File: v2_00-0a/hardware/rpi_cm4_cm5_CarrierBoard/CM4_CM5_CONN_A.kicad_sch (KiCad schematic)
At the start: 2 parts, among them J6 DF40HC(3.0)-100DS-0.4V(58), U17 Raspberry PI CM4 and CM5 symb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

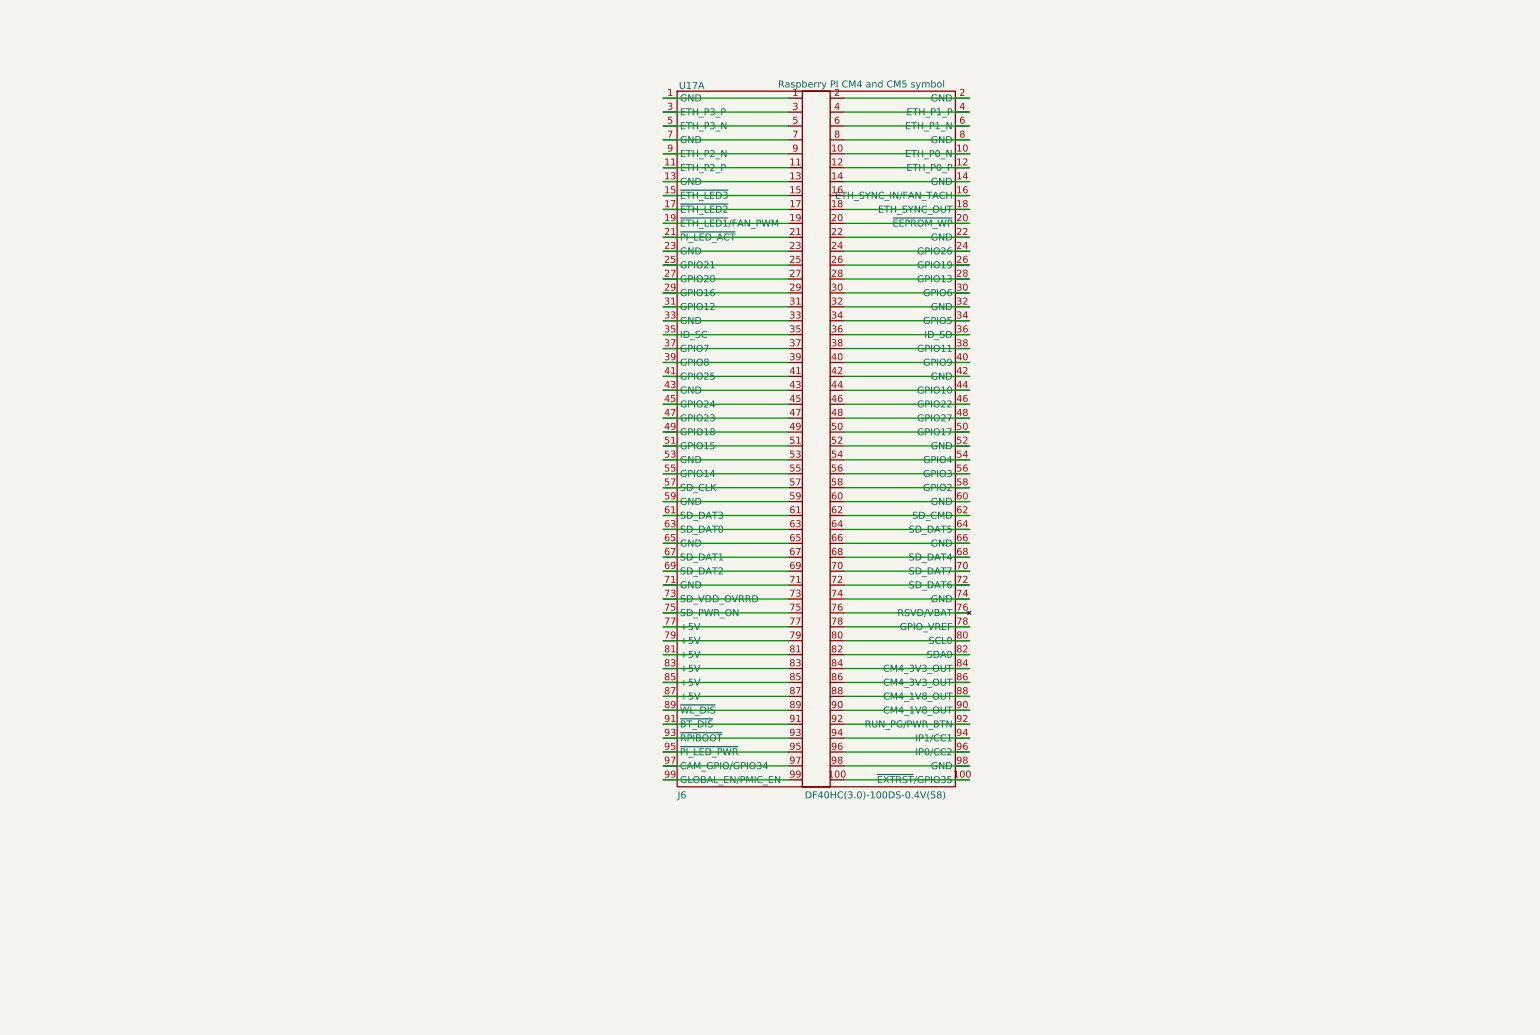
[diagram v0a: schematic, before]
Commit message: Update schematics (several new hierarchical pages, updates bus labels)
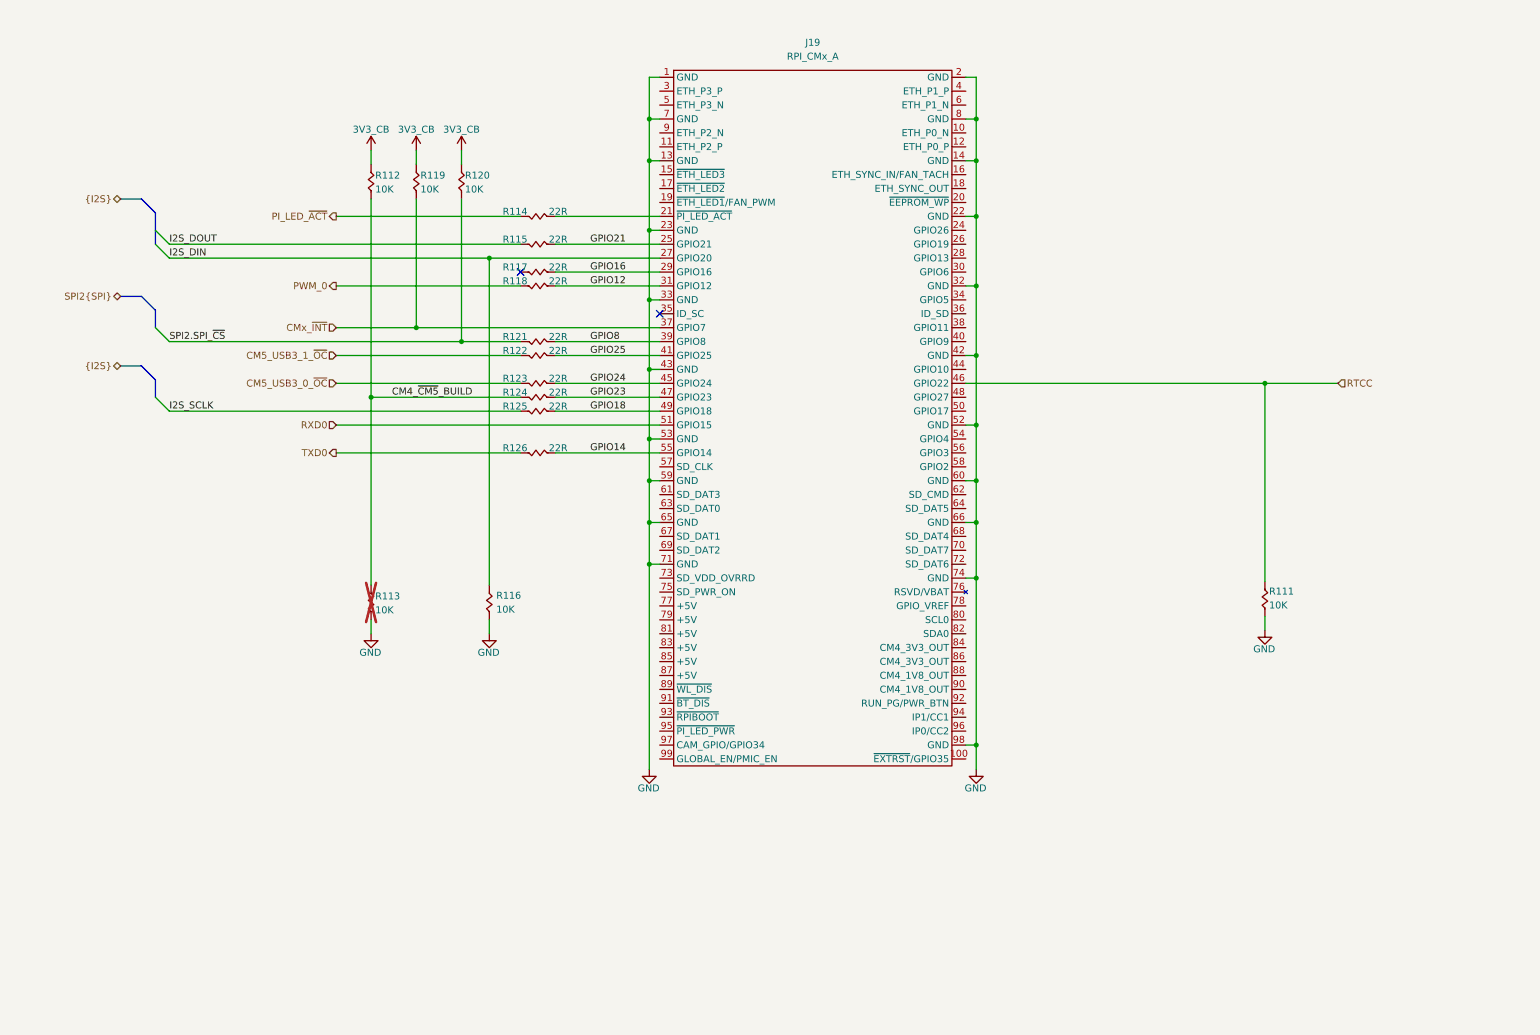
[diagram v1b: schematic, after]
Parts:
- removed J6: DF40HC(3.0)-100DS-0.4V(58), footprint:DF40HC(3.0)-100DS-0.4V, symbol KicadCompDb:Connector/CONN_00007
- removed U17: Raspberry PI CM4 and CM5 symbol, rPI_CM4_CM5, symbol KiCad_Lib_Symbols:RPI_CM4_CM5
- added J19: RPI_CMx_A, footprint:DF40HC(3.0)-100DS-0.4V, symbol KicadCompDb:Connector/CONN_00014
- added R111, R112, R113, R116, R119, R120: 10K, footprint:RES_0402, symbol KicadCompDb:Resistors/RES_SMT_00013
- added R114, R115, R117, R118, R121, R122, R123, R124, R125, R126: 22R, footprint:RES_0402, symbol KicadCompDb:Resistors/RES_SMT_00015
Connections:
- new net: J19.21 (~{PI_LED_ACT}), R114.1
- new net 3V3_CB: R112.2, R119.2, R120.2
- new net CM4_~{CM5}_BUILD: R112.1, R113.2, R124.2
- new net CM5_USB3_0_~{OC}: R123.2
- new net CM5_USB3_1_~{OC}: R122.2
- new net CMx_~{INT}: J19.37 (GPIO7), R119.1
- new net GND: J19.1 (GND), J19.13 (GND), J19.14 (GND), J19.2 (GND), J19.22 (GND), J19.23 (GND), J19.32 (GND), J19.33 (GND), J19.42 (GND), J19.43 (GND), J19.52 (GND), J19.53 (GND), J19.59 (GND), J19.60 (GND), J19.65 (GND), J19.66 (GND), J19.7 (GND), J19.71 (GND), J19.74 (GND), J19.8 (GND), J19.98 (GND), R111.1, R113.1, R116.1
- new net GPIO12: J19.31 (GPIO12), R118.1
- new net GPIO14: J19.55 (GPIO14), R126.1
- new net GPIO16: J19.29 (GPIO16), R117.1
- new net GPIO18: J19.49 (GPIO18), R125.1
- new net GPIO21: J19.25 (GPIO21), R115.1
- new net GPIO23: J19.47 (GPIO23), R124.1
- new net GPIO24: J19.45 (GPIO24), R123.1
- new net GPIO25: J19.41 (GPIO25), R122.1
- new net GPIO8: J19.39 (GPIO8), R121.1
- new net I2S_DIN: J19.27 (GPIO20), R116.2
- new net I2S_DOUT: R115.2
- new net I2S_SCLK: R125.2
- new net PI_LED_~{ACT}: R114.2
- new net PWM_0: R118.2
- new net RTCC: J19.46 (GPIO22), R111.2
- new net RXD0: J19.51 (GPIO15)
- new net SPI2.SPI_~{CS}: R120.1, R121.2
- new net TXD0: R126.2
- no-connect marks 0 -> 2

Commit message: Add new page and update schematics
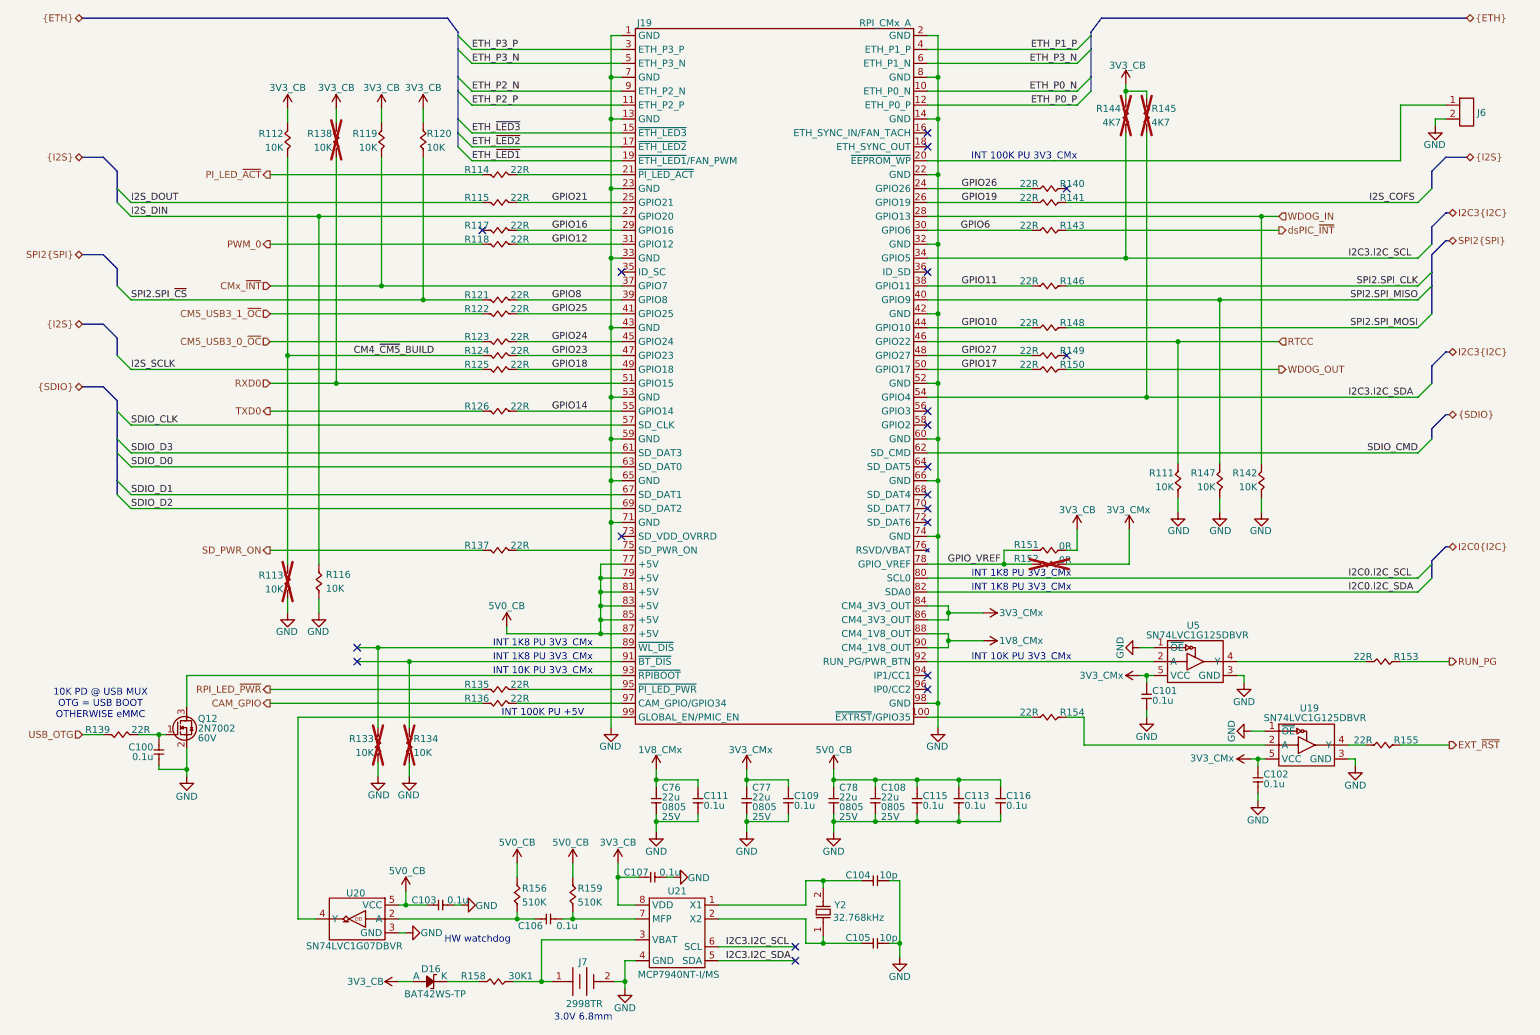
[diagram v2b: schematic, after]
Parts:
- added C100, C101, C102, C103, C106, C107, C109, C111, C113, C115, C116: 0.1u, footprint:CAP_NONPOL_0402, symbol KicadCompDb:Capacitors/CAP_CER_SMT_00001
- added C104, C105: 10p, footprint:CAP_NONPOL_0402, symbol KicadCompDb:Capacitors/CAP_CER_SMT_00006
- added C108, C76, C77, C78: 22u, footprint:CAP_NONPOL_0805, symbol KicadCompDb:Capacitors/CAP_CER_SMT_00011
- added D16: BAT42WS-TP, footprint:SOD-323, symbol KicadCompDb:Diodes/DIODE_00006
- added J6: M20-9990245, footprint:HEADER_2P_2_54MM, symbol KicadCompDb:Connector/CONN_00003
- added J7: 2998TR, 2998TR, symbol KicadCompDb:Miscellaneous/MISC_00005
- added Q12: 2N7002, footprint:SOT-23-3, symbol KicadCompDb:Mosfet/MOSFET_00001
- added R133, R134, R138, R142, R147: 10K, footprint:RES_0402, symbol KicadCompDb:Resistors/RES_SMT_00013
- added R135, R136, R137, R139, R140, R141, R143, R146, R148, R149, R150, R153, R154, R155: 22R, footprint:RES_0402, symbol KicadCompDb:Resistors/RES_SMT_00015
- added R144, R145: 4K7, footprint:RES_0402, symbol KicadCompDb:Resistors/RES_SMT_00010
- added R151, R152: 0R, footprint:RES_0402, symbol KicadCompDb:Resistors/RES_SMT_00001
- added R156, R159: 510K, footprint:RES_0402, symbol KicadCompDb:Resistors/RES_SMT_00020
- added R158: 30K1, footprint:RES_0402, symbol KicadCompDb:Resistors/RES_SMT_00016
- added U19, U5: SN74LVC1G125DBVR, footprint:SOT-23-5, symbol KicadCompDb:Logic/LOGIC_00001
- added U20: SN74LVC1G07DBVR, footprint:SOT-23-5, symbol KicadCompDb:Logic/LOGIC_00002
- added U21: MCP7940NT-I/MS, footprint:MSOP-8, symbol KicadCompDb:Digital/DIGITAL_00001
- added Y2: 32.768kHz, footprint:2-SMD_3_2mmx1_5mm, symbol KicadCompDb:Crystals/CRYSTAL_00003
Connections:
- net 3V3_CB: now also C107.1, D16.2 (A), R138.2, R144.2, R145.2, R151.2, U21.8 (VDD)
- net GND: now also C100.1, C101.1, C102.1, C103.2, C104.2, C105.2, C107.2, C108.1, C109.1, C111.1, C113.1, C115.1, C116.1, C76.1, C77.1, C78.1, J6.2, J7.2, Q12.2 (S), R133.1, R134.1, R142.1, R147.1, U19.1 (~{OE}), U19.3 (GND), U20.3 (GND), U21.4 (GND), U5.1 (~{OE}), U5.3 (GND)
- net RXD0: now also R138.1
- net ETH_P0_N: now reaches J19.10 (ETH_P0_N)
- net at J19.100 (~{EXTRST}/GPIO35): now also R154.1
- net ETH_P2_P: now reaches J19.11 (ETH_P2_P)
- net ETH_P0_P: now reaches J19.12 (ETH_P0_P)
- net ETH_~{LED3}: now reaches J19.15 (~{ETH_LED3})
- net ETH_~{LED2}: now reaches J19.17 (~{ETH_LED2})
- net ETH_~{LED1}: now reaches J19.19 (~{ETH_LED1}/FAN_PWM)
- net at J19.20 (~{EEPROM_WP}): now also J6.1
- net GPIO26: now reaches J19.24 (GPIO26)
- net GPIO26: now also R140.1
- net GPIO19: now reaches J19.26 (GPIO19)
- net GPIO19: now also R141.1
- net WDOG_IN: now reaches J19.28 (GPIO13)
- net WDOG_IN: now also R142.2
- net ETH_P3_P: now reaches J19.3 (ETH_P3_P)
- net GPIO6: now reaches J19.30 (GPIO6)
- net GPIO6: now also R143.1
- net I2C3.I2C_SCL: now reaches J19.34 (GPIO5)
- net I2C3.I2C_SCL: now also R144.1, U21.6 (SCL)
- net GPIO11: now reaches J19.38 (GPIO11)
- net GPIO11: now also R146.1
- net ETH_P1_P: now reaches J19.4 (ETH_P1_P)
- net SPI2.SPI_MISO: now reaches J19.40 (GPIO9)
- net SPI2.SPI_MISO: now also R147.2
- net GPIO10: now reaches J19.44 (GPIO10)
- net GPIO10: now also R148.1
- net GPIO27: now reaches J19.48 (GPIO27)
- net GPIO27: now also R149.1
- net ETH_P3_N: now reaches J19.5 (ETH_P3_N)
- net ETH_P3_N: now also J19.6 (ETH_P1_N)
- net GPIO17: now reaches J19.50 (GPIO17)
- net GPIO17: now also R150.1
- net I2C3.I2C_SDA: now reaches J19.54 (GPIO4)
- net I2C3.I2C_SDA: now also R145.1, U21.5 (SDA)
- net SDIO_CLK: now reaches J19.57 (SD_CLK)
- net SDIO_D3: now reaches J19.61 (SD_DAT3)
- net SDIO_CMD: now reaches J19.62 (SD_CMD)
- net SDIO_D0: now reaches J19.63 (SD_DAT0)
- net SDIO_D1: now reaches J19.67 (SD_DAT1)
- net SDIO_D2: now reaches J19.69 (SD_DAT2)
- net at J19.75 (SD_PWR_ON): now also R137.1
- net 5V0_CB: now reaches J19.77 (+5V)
- net 5V0_CB: now also J19.79 (+5V), J19.81 (+5V), J19.83 (+5V), J19.85 (+5V), J19.87 (+5V), C103.1, C108.2, C113.2, C115.2, C116.2, C78.2, R156.2, R159.2, U20.5 (VCC)
- net GPIO_VREF: now reaches J19.78 (GPIO_VREF)
- net GPIO_VREF: now also R151.1, R152.1
- net I2C0.I2C_SCL: now reaches J19.80 (SCL0)
- net I2C0.I2C_SDA: now reaches J19.82 (SDA0)
- net 3V3_CMx: now reaches J19.84 (CM4_3V3_OUT)
- net 3V3_CMx: now also J19.86 (CM4_3V3_OUT), C101.2, C102.2, C109.2, C77.2, R152.2, U19.5 (VCC), U5.5 (VCC)
- net 1V8_CMx: now reaches J19.88 (CM4_1V8_OUT)
- net 1V8_CMx: now also J19.90 (CM4_1V8_OUT), C111.2, C76.2
- net at J19.89 (~{WL_DIS}): now also R133.2
- net ETH_P2_N: now reaches J19.9 (ETH_P2_N)
- net at J19.91 (~{BT_DIS}): now also R134.2
- net at J19.92 (RUN_PG/PWR_BTN): now also U5.2 (A)
- net at J19.93 (~{RPIBOOT}): now also Q12.3 (D)
- net at J19.95 (~{PI_LED_PWR}): now also R135.1
- net at J19.97 (CAM_GPIO/GPIO34): now also R136.1
- net at J19.99 (GLOBAL_EN/PMIC_EN): now also U20.4 (Y)
- new net: R154.2, U19.2 (A)
- new net: J7.1, R158.1, U21.3 (VBAT)
- new net: D16.1 (K), R158.2
- new net: C106.1, R156.1, U20.2 (A)
- new net: C106.2, R159.1, U21.7 (MFP)
- new net: C104.1, U21.1 (X1), Y2.2 (XO)
- new net: R153.1, U5.4 (Y)
- new net: C105.1, U21.2 (X2), Y2.1 (XI)
- new net: R155.1, U19.4 (Y)
- new net: C100.2, Q12.1 (G), R139.1
- new net CAM_GPIO: R136.2
- new net EXT_~{RST}: R155.2
- new net I2S_COFS: R141.2
- new net RPI_LED_~{PWR}: R135.2
- new net RUN_PG: R153.2
- new net SD_PWR_ON: R137.2
- new net SPI2.SPI_CLK: R146.2
- new net SPI2.SPI_MOSI: R148.2
- new net USB_OTG: R139.2
- new net WDOG_OUT: R150.2
- new net dsPIC_~{INT}: R143.2
- no-connect marks 2 -> 20
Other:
- note added: "10K PD @ USB MUX OTG = USB BOOT OTHERWISE eMMC"
- note added: "3.0V 6.8mm"
- note added: "HW watchdog"
- note added: "INT 100K PU +5V"
- note added: "INT 100K PU 3V3_CMx"
- note added: "INT 10K PU 3V3_CMx"
- note added: "INT 1K8 PU 3V3_CMx"
- moved on the sheet: J19, R111, R112, R113, R114, R115, R116, R117, R118, R119, R120, R121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

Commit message: Add design notes (power table) and latest changes to power supply and power input
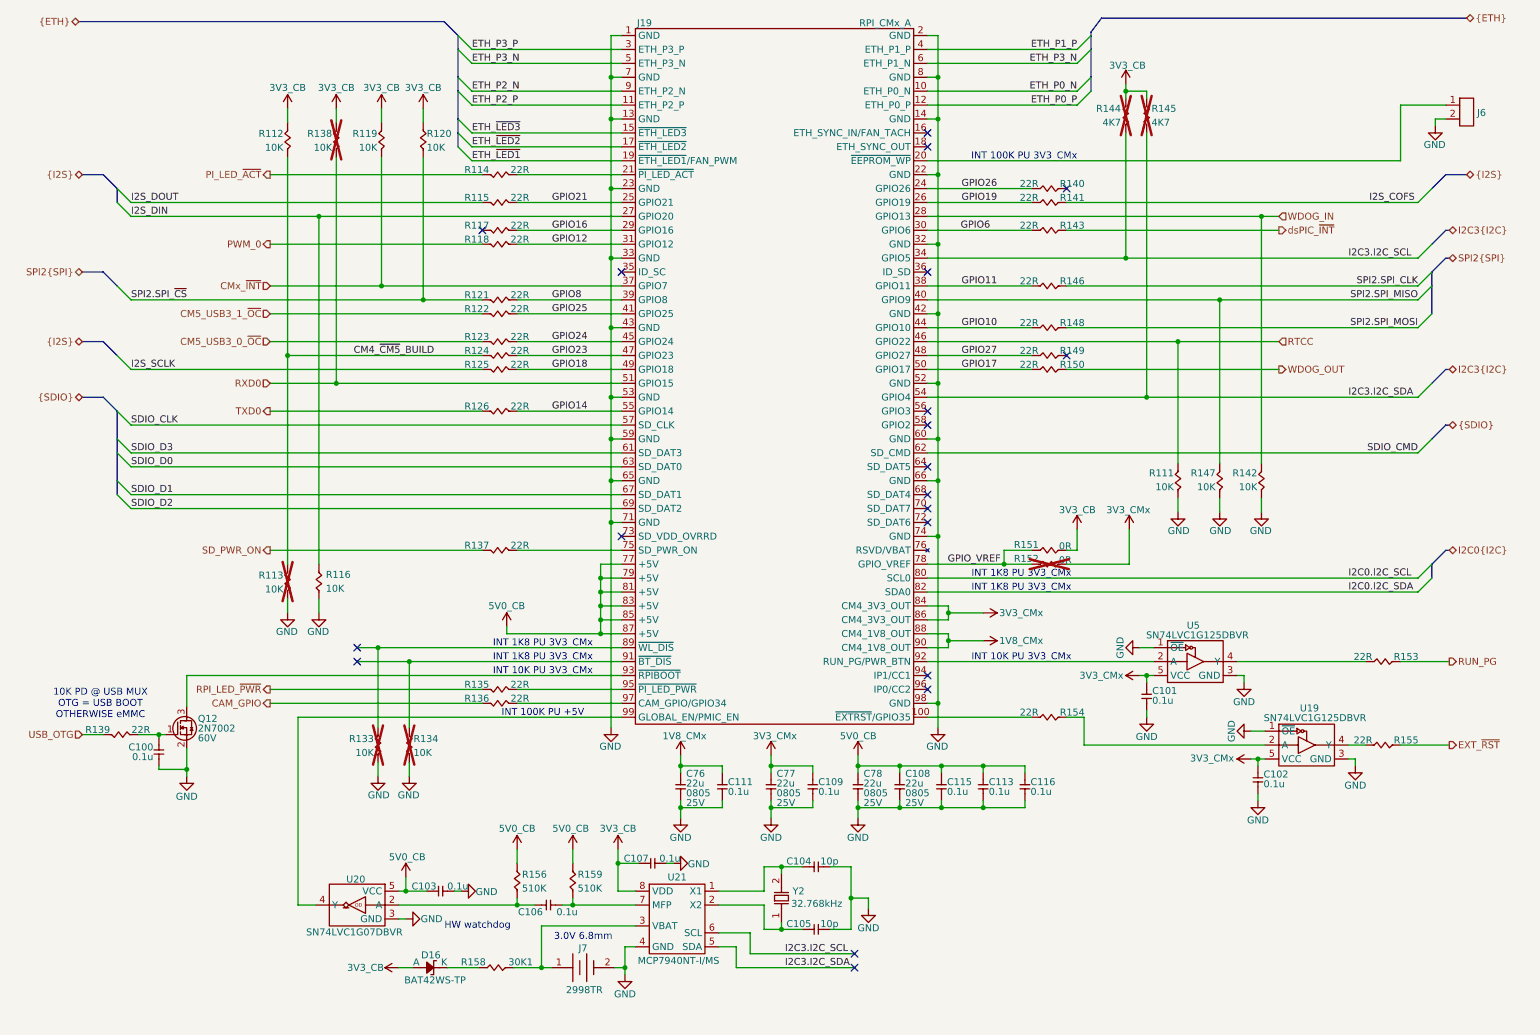
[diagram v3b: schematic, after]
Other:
- moved on the sheet: C103, C104, C105, C106, C107, C108, C109, C111, C113, C115, C116, C76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
